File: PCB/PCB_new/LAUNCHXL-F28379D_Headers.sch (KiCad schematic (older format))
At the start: 10 parts, among them U1 AMP_DUE_SCH, U2 AMP_DUE_SCH

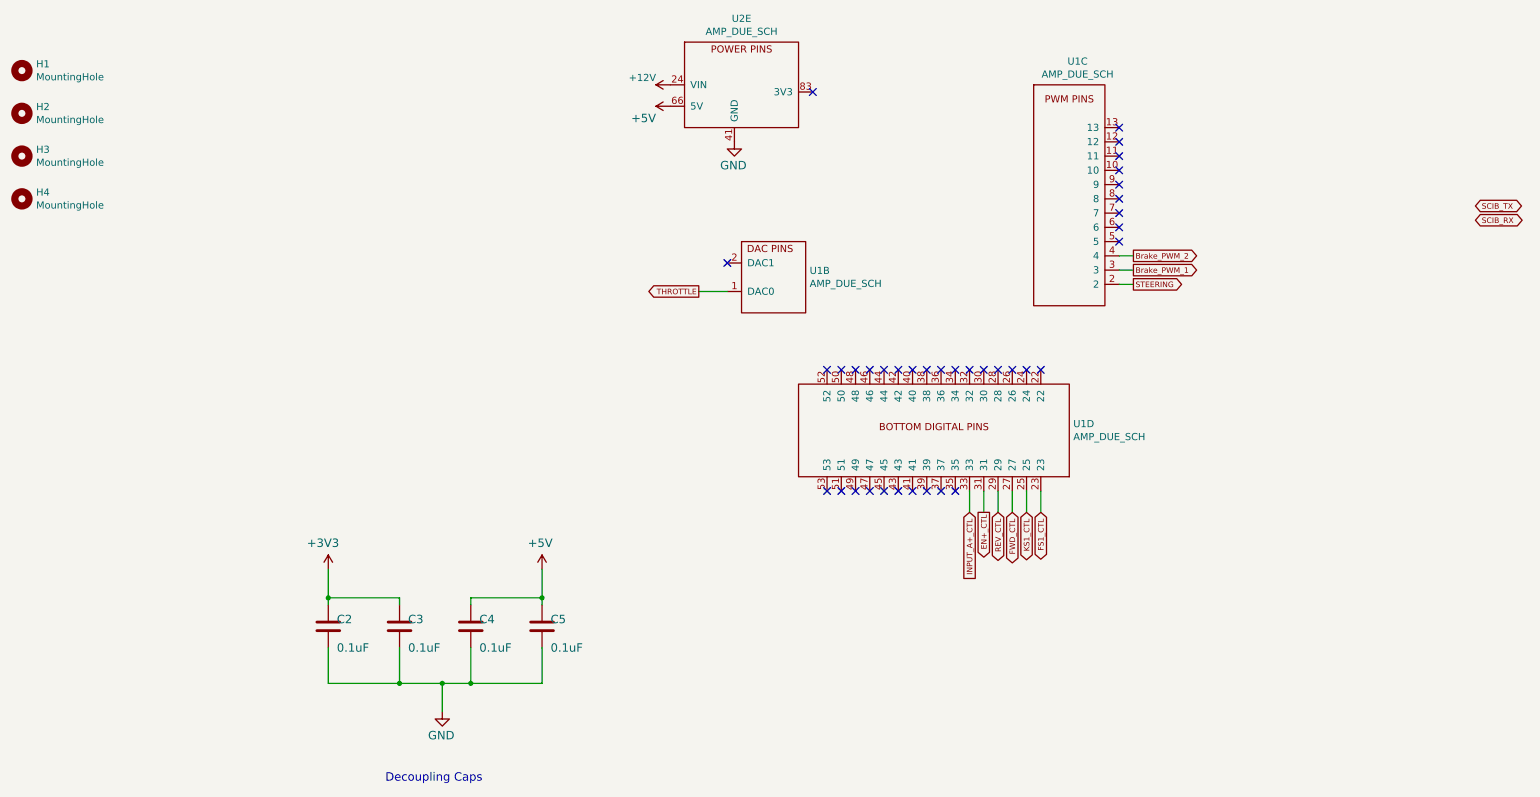
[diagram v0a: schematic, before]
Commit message: changed board to work with arduino due
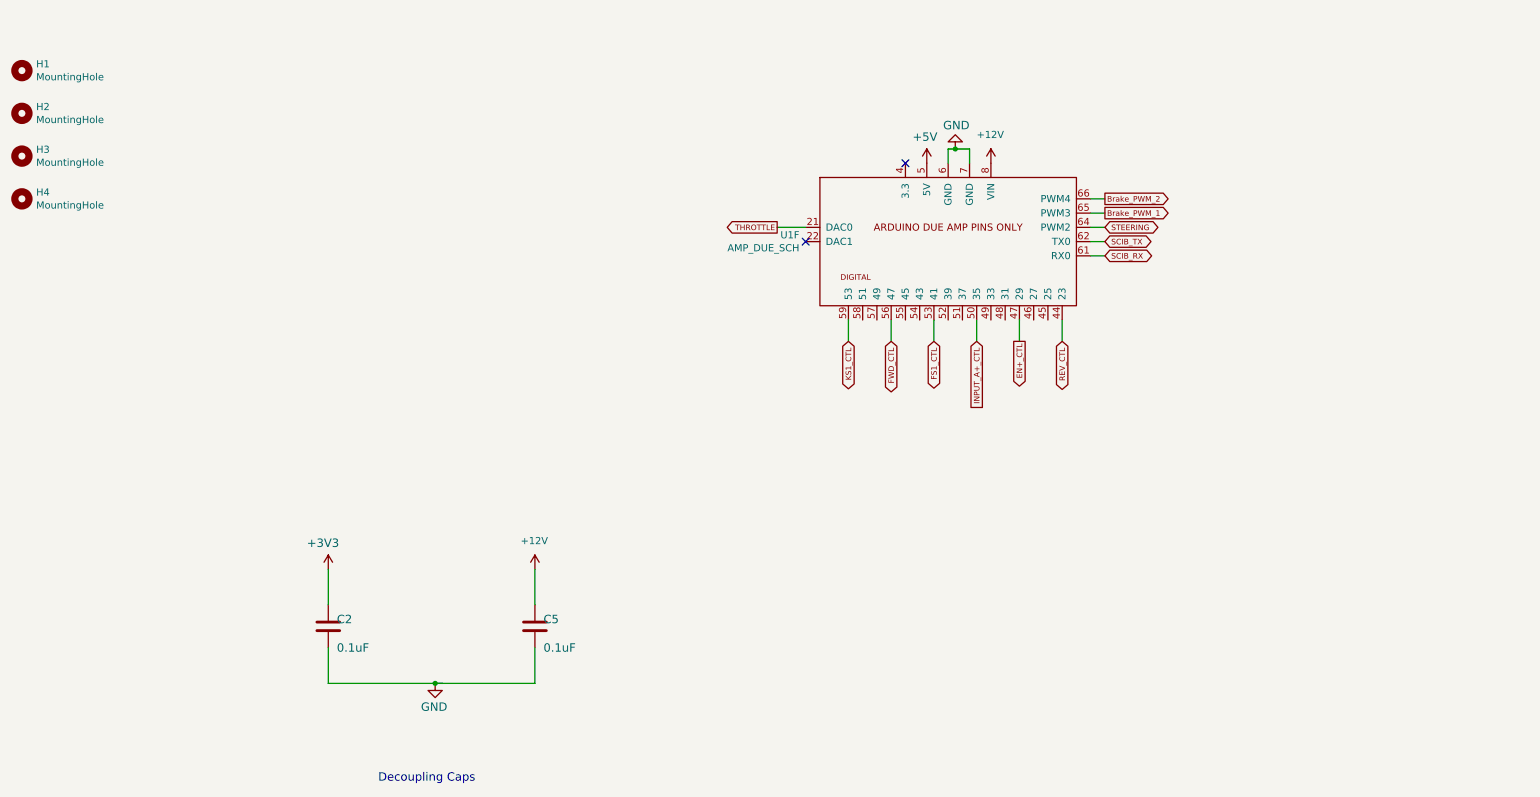
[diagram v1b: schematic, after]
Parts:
- removed C3, C4: 0.1uF, Capacitor_SMD:C_0805_2012Metric_Pad1.15x1.40mm_HandSolder, symbol Device:C
- removed U1, U2: AMP_DUE_SCH, DUE Footprint:Arduino DUE, symbol PCB_2020:AMP_DUE_SCH
- added U1: AMP_DUE_SCH, Drivetrain_control:Arduino DUE, symbol PCB_2020:AMP_DUE_SCH
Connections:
- net +12V: now also C5.1, U1.8 (VIN)
- net +5V: now also U1.5 (5V); no longer C5.1
- net Brake_PWM_1: now also U1.65 (PWM3)
- net Brake_PWM_2: now also U1.66 (PWM4)
- net EN+_CTL: now also U1.47 (29)
- net FS1_CTL: now also U1.53 (41)
- net FWD_CTL: now also U1.56 (47)
- net GND: now also U1.6 (GND), U1.7 (GND)
- net INPUT_A+_CTL: now also U1.50 (35)
- net KS1_CTL: now also U1.59 (53)
- net REV_CTL: now also U1.44 (23)
- net SCIB_RX: now also U1.61 (RX0)
- net SCIB_TX: now also U1.62 (TX0)
- net STEERING: now also U1.64 (PWM2)
- net THROTTLE: now also U1.21 (DAC0)
- no-connect marks 37 -> 2
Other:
- moved on the sheet: C5

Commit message: moved all connections to the right side
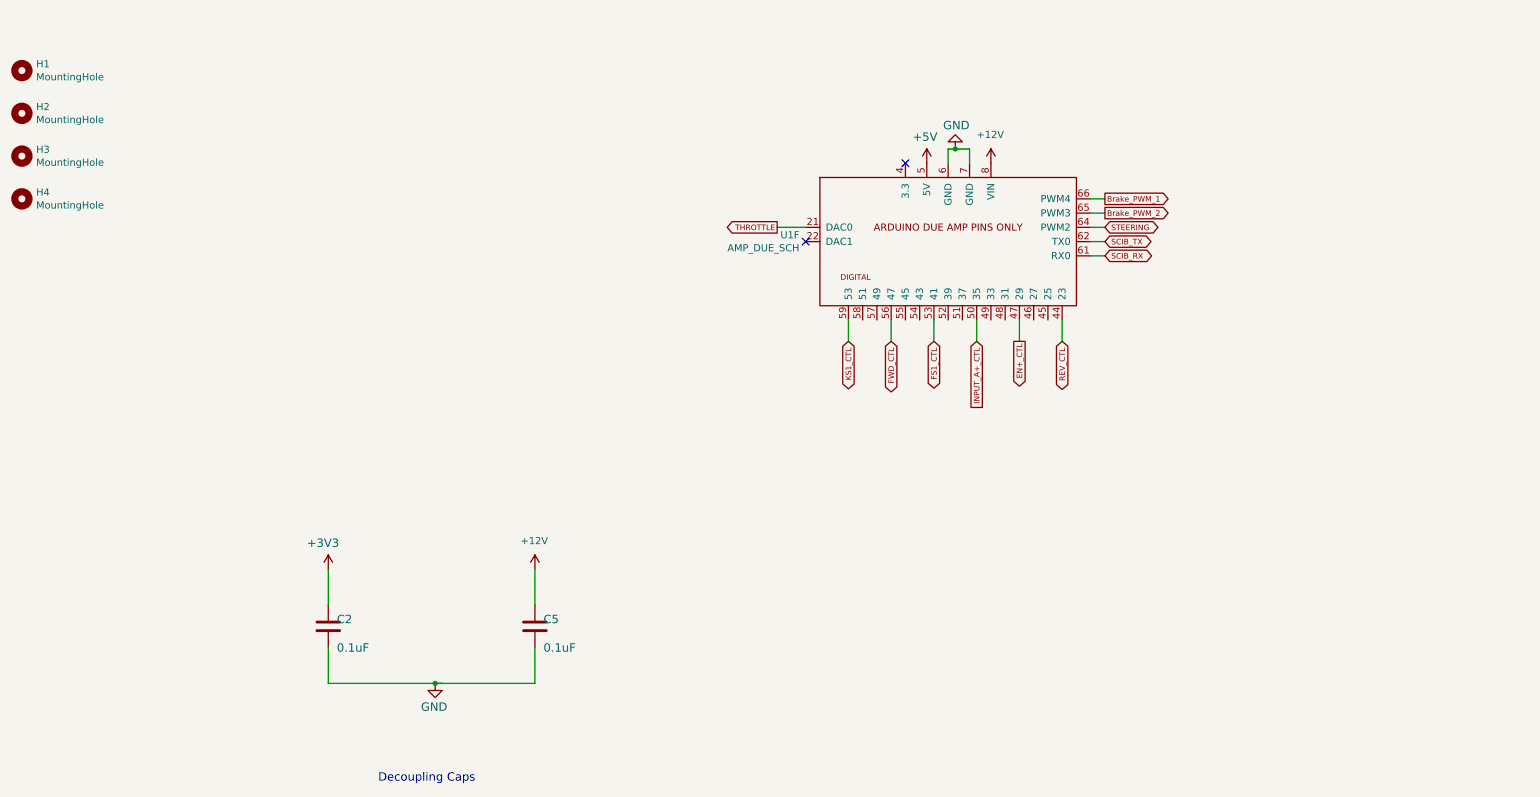
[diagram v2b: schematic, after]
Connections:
- wire segments 24 -> 23
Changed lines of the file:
@@
 Text GLabel 8750 3400 2    39   BiDi ~ 0
 SCIB_TX
+Text GLabel 8750 3100 2    39   Output ~ 0
+Brake_PWM_1
 Text GLabel 8750 3200 2    39   Output ~ 0
-Brake_PWM_1
-Text GLabel 8750 3100 2    39   Output ~ 0
 Brake_PWM_2
 Wire Wire Line
@@
 $EndComp
 Wire Wire Line
-	4050 6500 4100 6500
-Wire Wire Line
 	4750 5700 4750 5950
-Wire Wire Line
-	4100 6500 4750 6500
 Wire Wire Line
 	3300 6250 3300 6500
@@
 Wire Wire Line
 	4050 6500 4100 6500
+Wire Wire Line
+	4050 6500 4750 6500
 $EndSCHEMATC
